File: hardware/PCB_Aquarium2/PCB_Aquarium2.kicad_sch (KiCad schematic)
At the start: 16 parts, among them SW1 SW_SPST, U1 STM32G474RETx

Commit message: PCBs v3
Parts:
- added L1: 39n, Inductor_SMD:L_0805_2012Metric, symbol Device:L
- C1, C10, C5: footprint Capacitor_SMD:C_0402_1005Metric -> Capacitor_SMD:C_0603_1608Metric
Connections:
- net +3.3V: now also L1.1, L1.2
- net ADC1_IN10_PH: now reaches U1.5 (PF0)
- net GPIO_PH: no longer names the net of U1.2 (PC13)
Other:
- moved on the sheet: C10, C9
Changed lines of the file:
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@@
 	)
 	(junction
+		(at 157.48 38.1)
+		(diameter 0)
+		(color 0 0 0 0)
+	)
+	(junction
 		(at 97.79 38.1)
 		(diameter 0)
@@
 	)
 	(junction
+		(at 142.24 38.1)
+		(diameter 0)
+		(color 0 0 0 0)
+	)
+	(junction
 		(at 152.4 46.99)
 		(diameter 0)
@@
 	)
 	(junction
-		(at 162.56 39.37)
+		(at 162.56 38.1)
 		(diameter 0)
 		(color 0 0 0 0)
@@
 	)
 	(junction
-		(at 172.72 45.72)
+		(at 172.72 44.45)
 		(diameter 0)
 		(color 0 0 0 0)
@@
 	)
 	(no_connect
-		(at 132.08 66.04)
+		(at 132.08 111.76)
 	)
 	(wire
@@
 	(wire
 		(pts
-			(xy 172.72 44.45) (xy 172.72 45.72)
+			(xy 172.72 43.18) (xy 172.72 44.45)
 		)
 		(stroke
@@
 	(wire
 		(pts
-			(xy 157.48 39.37) (xy 157.48 46.99)
+			(xy 157.48 38.1) (xy 157.48 46.99)
 		)
 		(stroke
@@
 	(wire
 		(pts
-			(xy 172.72 45.72) (xy 162.56 45.72)
+			(xy 172.72 44.45) (xy 162.56 44.45)
 		)
 		(stroke
@@
 	(wire
 		(pts
-			(xy 162.56 39.37) (xy 157.48 39.37)
+			(xy 162.56 38.1) (xy 157.48 38.1)
+		)
+		(stroke
+			(width 0)
+			(type default)
+		)
+	)
+	(wire
+		(pts
+			(xy 142.24 38.1) (xy 146.05 38.1)
 		)
 		(stroke
@@
 	(wire
 		(pts
-			(xy 162.56 39.37) (xy 172.72 39.37)
+			(xy 162.56 38.1) (xy 172.72 38.1)
 		)
 		(stroke
@@
 	(wire
 		(pts
-			(xy 162.56 45.72) (xy 162.56 44.45)
+			(xy 162.56 44.45) (xy 162.56 43.18)
 		)
 		(stroke
@@
 	(wire
 		(pts
-			(xy 172.72 45.72) (xy 172.72 46.99)
+			(xy 172.72 44.45) (xy 172.72 45.72)
 		)
 		(stroke
@@
 		)
 	)
+	(wire
+		(pts
+			(xy 153.67 38.1) (xy 157.48 38.1)
+		)
+		(stroke
+			(width 0)
+			(type default)
+		)
+	)
 	(global_label "SPI2_MOSI"
 		(shape input)
@@
 		)
 	)
+	(global_label "ADC1_IN10_PH"
+		(shape input)
+		(at 132.08 66.04 180)
+		(fields_autoplaced yes)
+		(effects
+			(font
+				(size 1.27 1.27)
+			)
+			(justify right)
+		)
+		(property "Intersheetrefs" "${INTERSHEET_REFS}"
+			(at 115.3667 66.04 0)
+			(effects
+				(font
+					(size 1.27 1.27)
+				)
+				(justify right)
+				(hide yes)
+			)
+		)
+	)
 	(global_label "GPIO_BTN_5"
 		(shape input)
@@
 		)
 	)
-	(global_label "GPIO_PH"
+	(global_label "ADC1_IN10_PH"
 		(shape input)
 		(at 251.46 148.59 180)
@@
 		)
 		(property "Intersheetrefs" "${INTERSHEET_REFS}"
-			(at 240.4314 148.59 0)
+			(at 234.7467 148.59 0)
 			(effects
 				(font
@@
 		)
 	)
-	(global_label "GPIO_PH"
-		(shape input)
-		(at 132.08 111.76 180)
-		(fields_autoplaced yes)
-		(effects
-			(font
-				(size 1.27 1.27)
-			)
-			(justify right)
-		)
-		(property "Intersheetrefs" "${INTERSHEET_REFS}"
-			(at 121.0514 111.76 0)
-			(effects
-				(font
-					(size 1.27 1.27)
-				)
-				(justify right)
-				(hide yes)
-			)
-		)
-	)
 	(global_label "GPIO_WaterSensor_2"
 		(shape input)
@@
 		(lib_name "GND_5")
 		(lib_id "power:GND")
-		(at 172.72 46.99 0)
+		(at 172.72 45.72 0)
 		(unit 1)
 		(exclude_from_sim no)
@@
 		(fields_autoplaced yes)
 		(property "Reference" "#PWR07"
-			(at 172.72 53.34 0)
+			(at 172.72 52.07 0)
 			(effects
 				(font
@@
 		)
 		(property "Value" "GND"
-			(at 172.72 52.07 0)
+			(at 172.72 50.8 0)
 			(effects
 				(font
@@
 		)
 		(property "Footprint" ""
-			(at 172.72 46.99 0)
+			(at 172.72 45.72 0)
 			(effects
 				(font
@@
 		)
 		(property "Datasheet" ""
-			(at 172.72 46.99 0)
+			(at 172.72 45.72 0)
 			(effects
 				(font
@@
 		)
 		(property "Description" "Power symbol creates a global label with name \"GND\" , ground"
-			(at 172.72 46.99 0)
+			(at 172.72 45.72 0)
 			(effects
 				(font
@@
 	)
 	(symbol
+		(lib_id "Device:L")
+		(at 149.86 38.1 90)
+		(unit 1)
+		(exclude_from_sim no)
+		(in_bom yes)
+		(on_board yes)
+		(dnp no)
+		(fields_autoplaced yes)
+		(property "Reference" "L1"
+			(at 149.86 33.02 90)
+			(effects
+				(font
+					(size 1.27 1.27)
+				)
+			)
+		)
+		(property "Value" "39n"
+			(at 149.86 35.56 90)
+			(effects
+				(font
+					(size 1.27 1.27)
+				)
+			)
+		)
+		(property "Footprint" "Inductor_SMD:L_0805_2012Metric"
+			(at 149.86 38.1 0)
+			(effects
+				(font
+					(size 1.27 1.27)
+				)
+				(hide yes)
+			)
+		)
+		(property "Datasheet" "~"
+			(at 149.86 38.1 0)
+			(effects
+				(font
+					(size 1.27 1.27)
+				)
+				(hide yes)
+			)
+		)
+		(property "Description" "Inductor"
+			(at 149.86 38.1 0)
+			(effects
+				(font
+					(size 1.27 1.27)
+				)
+				(hide yes)
+			)
+		)
+		(pin "1"
+		)
+		(pin "2"
+		)
+		(instances
+			(project ""
+				(path "/4f9429d5-fbb3-48e9-90dd-7ff0c2950e6f"
+					(reference "L1")
+					(unit 1)
+				)
+			)
+		)
+	)
+	(symbol
 		(lib_id "Device:C_Small")
 		(at 125.73 40.64 0)
@@
 	(symbol
 		(lib_id "Device:C_Small")
-		(at 162.56 41.91 0)
+		(at 162.56 40.64 0)
 		(unit 1)
 		(exclude_from_sim no)
@@
 		(fields_autoplaced yes)
 		(property "Reference" "C9"
-			(at 165.1 40.6462 0)
+			(at 165.1 39.3762 0)
 			(effects
 				(font
@@
 		)
 		(property "Value" "10n"
-			(at 165.1 43.1862 0)
+			(at 165.1 41.9162 0)
 			(effects
 				(font
@@
 		)
 		(property "Footprint" "Capacitor_SMD:C_0402_1005Metric"
-			(at 162.56 41.91 0)
+			(at 162.56 40.64 0)
 			(effects
 				(font
@@
 		)
 		(property "Datasheet" "~"
-			(at 162.56 41.91 0)
+			(at 162.56 40.64 0)
 			(effects
 				(font
@@
 		)
 		(property "Description" ""
-			(at 162.56 41.91 0)
+			(at 162.56 40.64 0)
 			(effects
 				(font
@@
 	(symbol
 		(lib_id "Device:C_Small")
-		(at 172.72 41.91 0)
+		(at 172.72 40.64 0)
 		(unit 1)
 		(exclude_from_sim no)
@@
 		(fields_autoplaced yes)
 		(property "Reference" "C10"
-			(at 175.26 40.6462 0)
+			(at 175.26 39.3762 0)
 			(effects
 				(font
@@
 		)
 		(property "Value" "1u"
-			(at 175.26 43.1862 0)
+			(at 175.26 41.9162 0)
 			(effects
 				(font
@@
 			)
 		)
-		(property "Footprint" "Capacitor_SMD:C_0402_1005Metric"
-			(at 172.72 41.91 0)
+		(property "Footprint" "Capacitor_SMD:C_0603_1608Metric"
+			(at 172.72 40.64 0)
 			(effects
 				(font
@@
 		)
 		(property "Datasheet" "~"
-			(at 172.72 41.91 0)
+			(at 172.72 40.64 0)
 			(effects
 				(font
@@
 		)
 		(property "Description" ""
-			(at 172.72 41.91 0)
+			(at 172.72 40.64 0)
 			(effects
 				(font
@@
 			)
 		)
-		(property "Footprint" "Capacitor_SMD:C_0402_1005Metric"
+		(property "Footprint" "Capacitor_SMD:C_0603_1608Metric"
 			(at 111.76 50.8 0)
 			(effects
@@
 			)
 		)
-		(property "Footprint" "Capacitor_SMD:C_0402_1005Metric"
+		(property "Footprint" "Capacitor_SMD:C_0603_1608Metric"
 			(at 90.17 40.64 0)
 			(effects

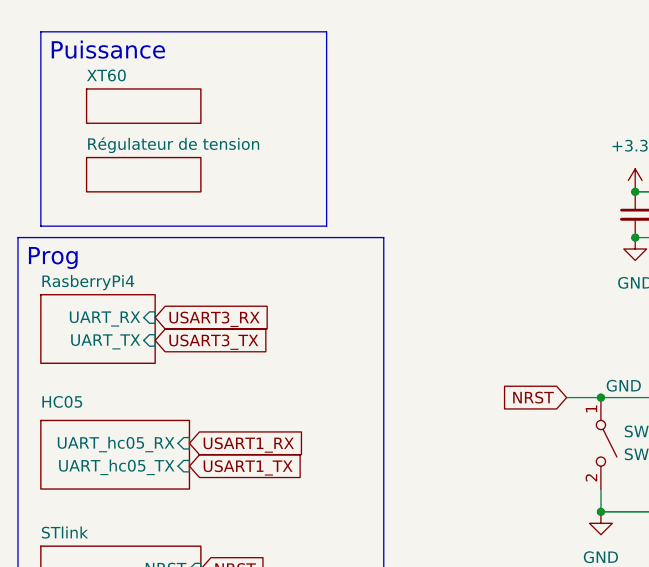
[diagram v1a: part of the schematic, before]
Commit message: ajoutpremiers fichiers python et maj JST XH pour la PI4
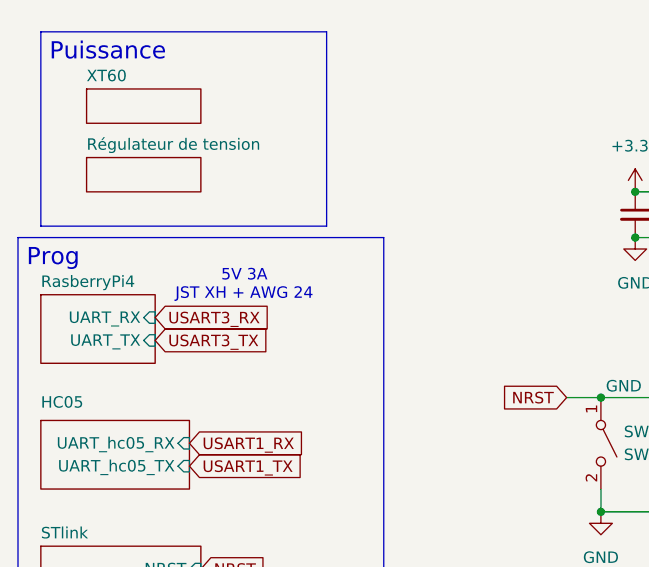
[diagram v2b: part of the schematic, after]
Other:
- note added: "5V 3A JST XH + AWG 24"
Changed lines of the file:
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@@
 	(generator_version "9.0")
 	(paper "A4")
+	(text "5V 3A\nJST XH + AWG 24"
+		(exclude_from_sim no)
+		(at 46.736 48.514 0)
+		(effects
+			(font
+				(size 1.27 1.27)
+			)
+		)
+	)
 	(text "4VDDx100n"
 		(exclude_from_sim no)
